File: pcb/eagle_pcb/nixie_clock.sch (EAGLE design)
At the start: 148 parts, among them J1 USB-C-VVERTICAL, J2 8, J3 8, J4 4, J5 4, J6 PH-2, Q1 IRLR3110ZPBF, Q2 BC817-25, Q3 BC817-25, Q4 BC817-25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

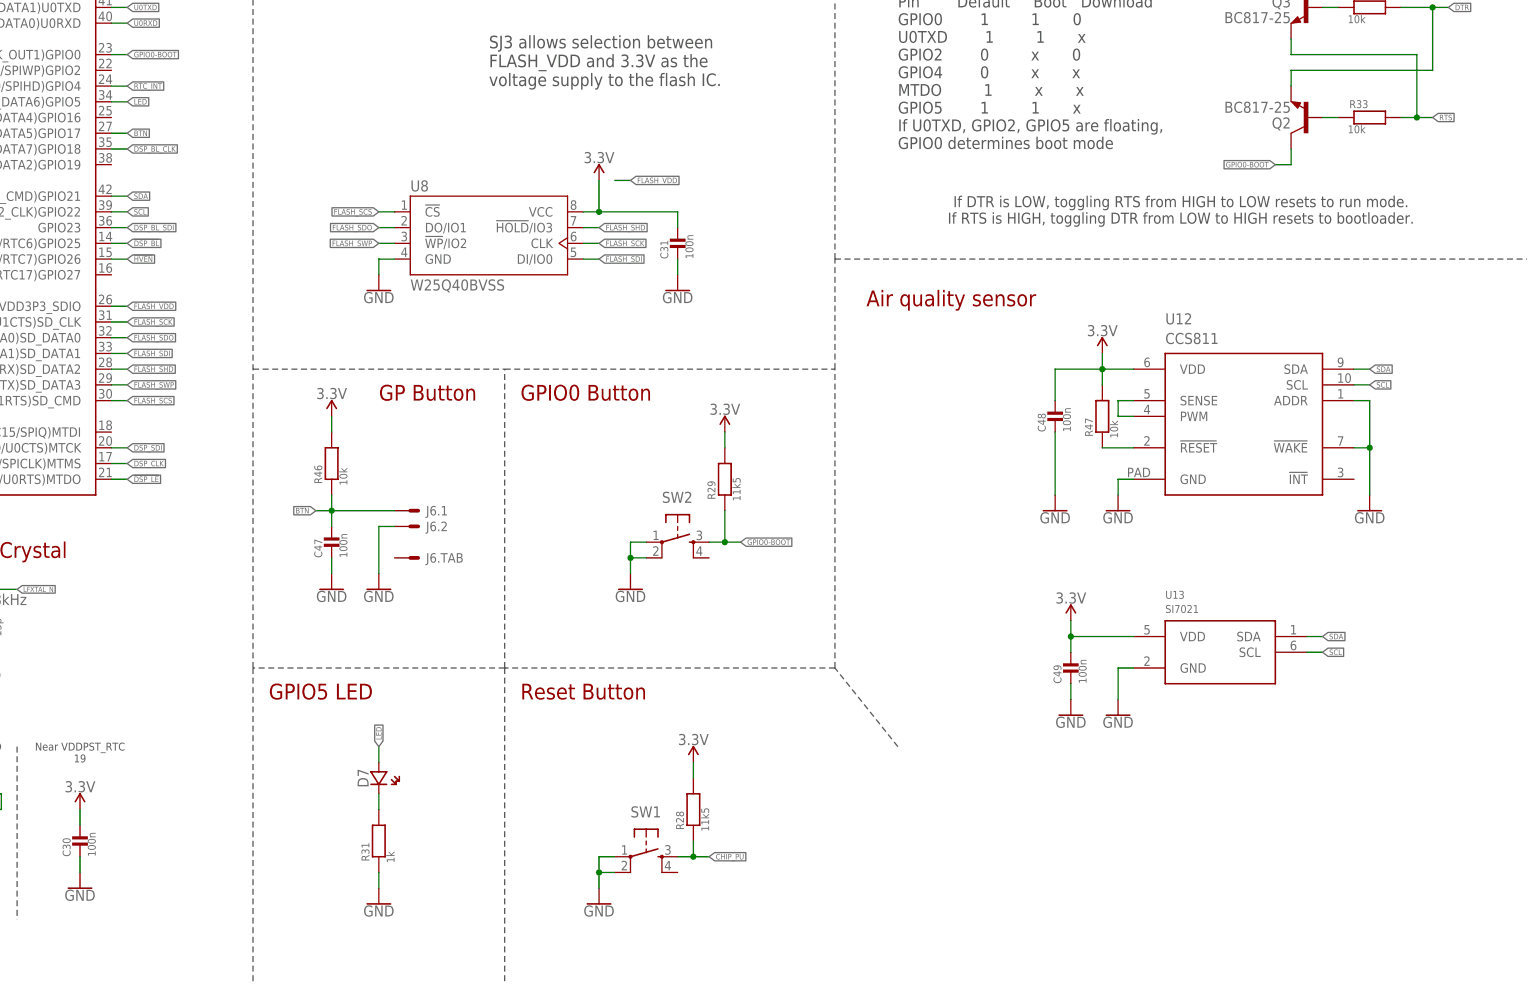
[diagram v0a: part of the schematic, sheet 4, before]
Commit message: added buzzer
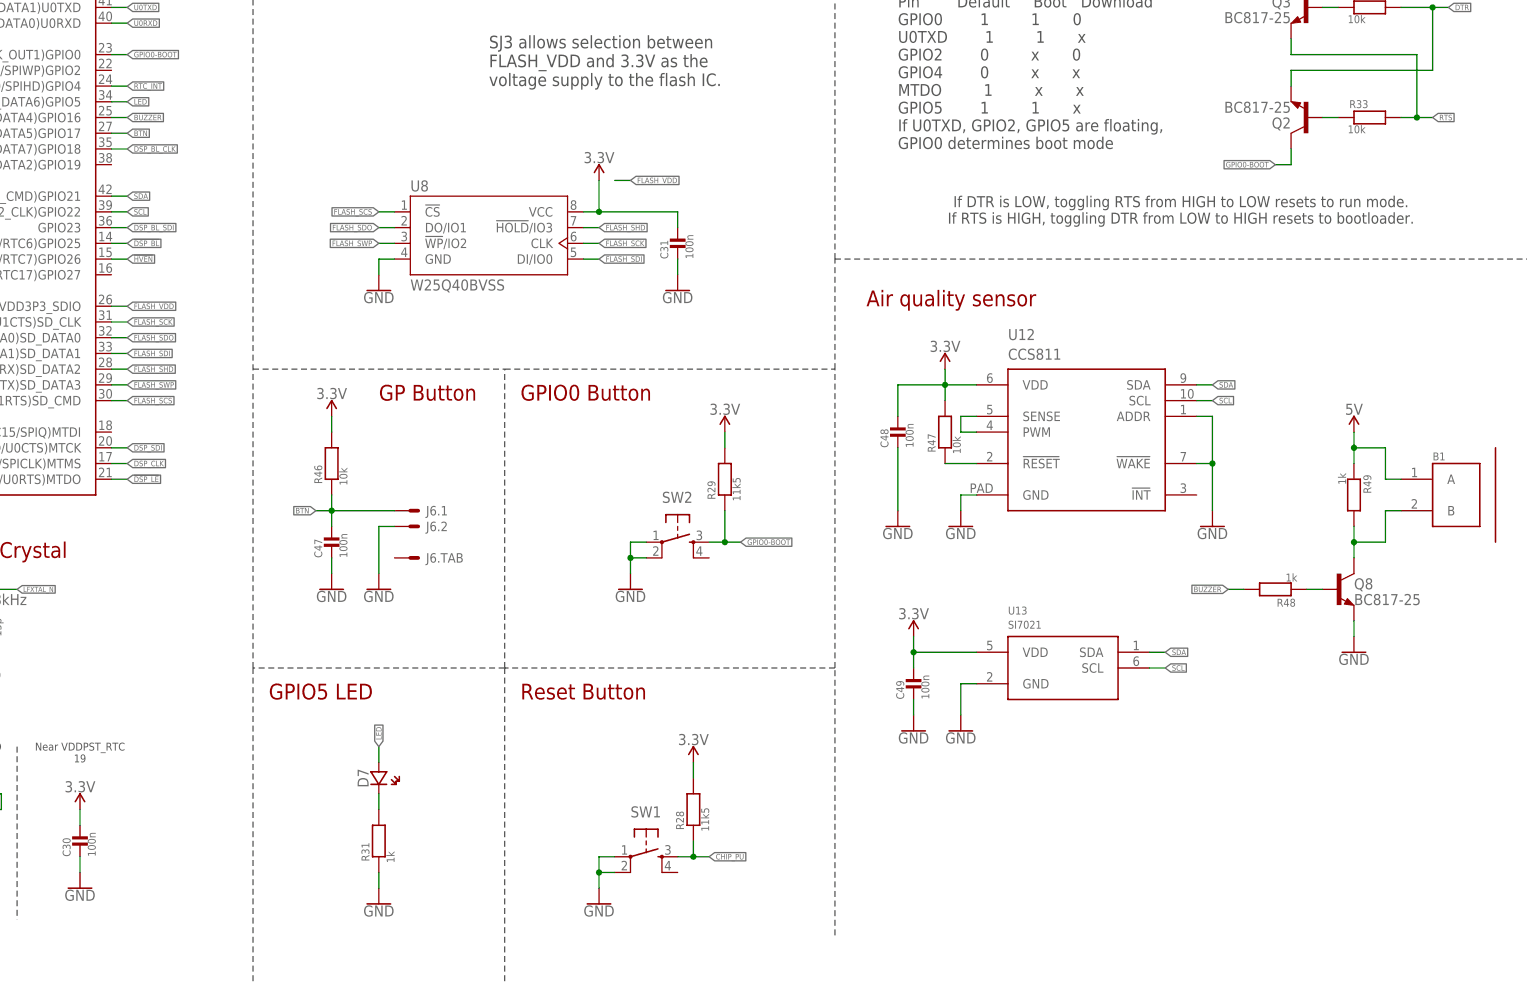
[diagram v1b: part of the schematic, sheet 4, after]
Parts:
- added B1: (no value), Eletromechanical > Buzzer:PKLCS1212E2400-R1
- added Q8: BC817-25, Semiconductors > Discrete Semiconductors > Transistors > Bipolar Transistors - BJT:BC817-25
- added R48, R49: 1k, Passive Components > Resistors > Chip Resistors:RESISTOR0603
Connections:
- new net BUZZER: R48.P$2, U1.(HS1_DATA4)GPIO16
- new net N$38: B1.B, Q8.C03, R49.P$2
- new net N$39: Q8.BA1, R48.P$1
- net 5V: now also B1.A, R49.P$1
- net GND: now also Q8.EM2
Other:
- moved on the sheet: C48, C49, R47, U12, U13
